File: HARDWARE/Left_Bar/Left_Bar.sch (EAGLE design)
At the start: 13 parts, among them J1 TRRS

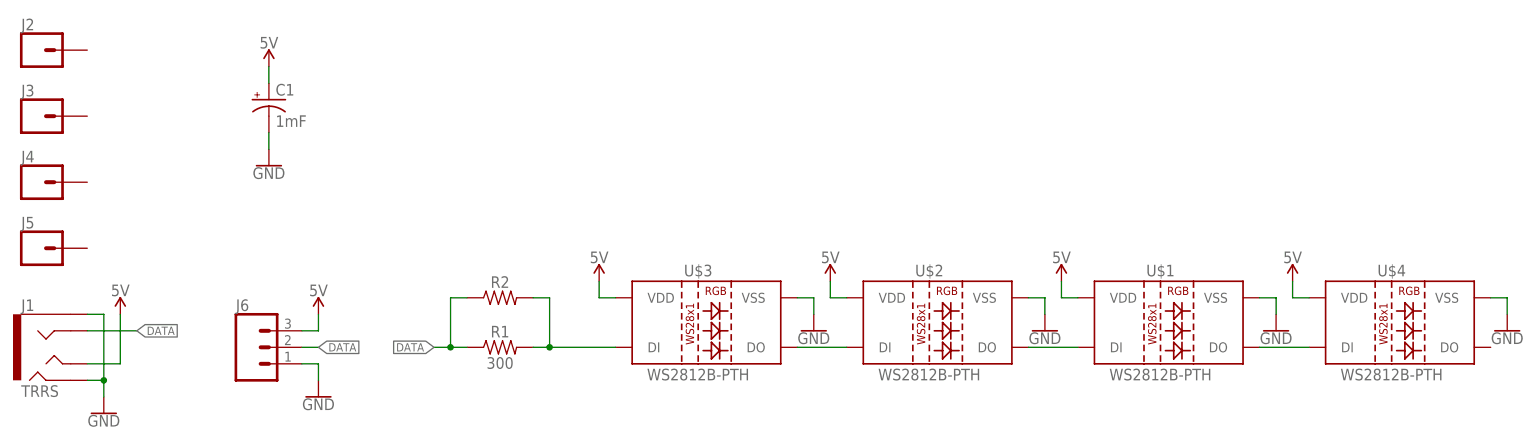
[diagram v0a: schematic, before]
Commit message: renames right and left, finished left
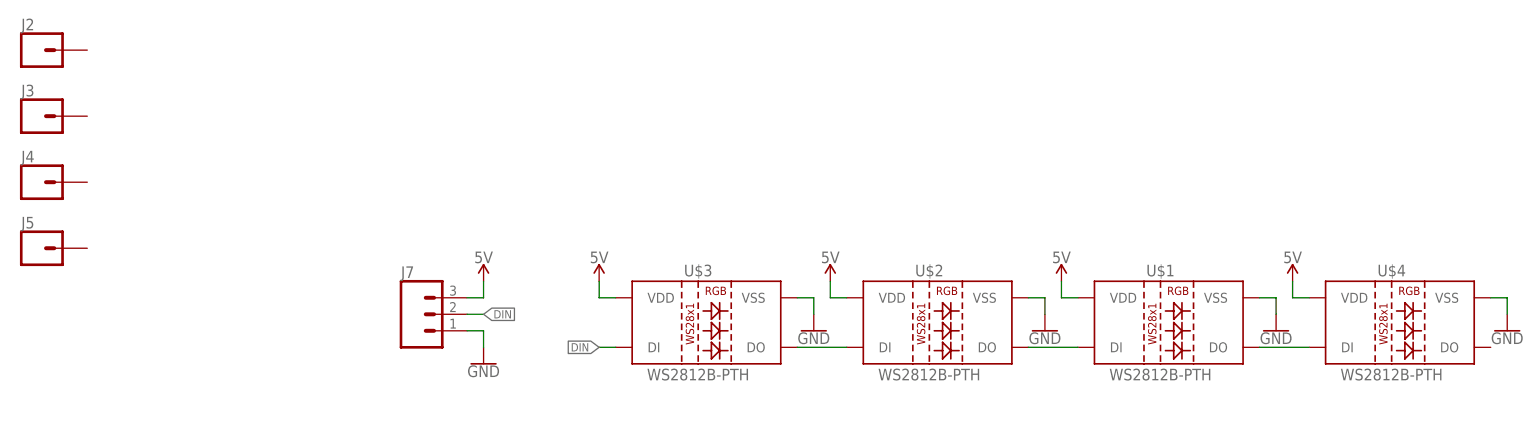
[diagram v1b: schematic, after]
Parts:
- removed C1: 1mF, SparkFun-Capacitors:1000UF-RADIAL-5MM-25V-20%
- removed J1: TRRS, SparkFun-Connectors:AUDIO_JACK_TRRSSMD_RA
- removed J6: (no value), SparkFun-Connectors:CONN_03
- removed R1: 300, SparkFun-Resistors:300OHM-0603-1/10W-1%
- removed R2: (no value), SparkFun-Resistors:RESISTORAXIAL-0.3
- added J7: (no value), SparkFun-Connectors:CONN_03
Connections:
- removed net DATA: J1.RING1, J6.2, R1.1, R2.1
- removed net N$2: R1.2, R2.2, U$3.DI
- new net DIN: J7.2, U$3.DI
- net 5V: now also J7.3; no longer C1.+, J1.TIP, J6.3
- net GND: now also J7.1; no longer C1.-, J1.EARTH, J1.RING2, J6.1
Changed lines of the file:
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@@
 </classes>
 <parts>
-<part name="J1" library="SparkFun-Connectors" deviceset="AUDIO_JACK_TRRS" device="SMD_RA" value="TRRS"/>
 <part name="U$1" library="SparkFun-LED" deviceset="WS2812B-PTH" device=""/>
 <part name="U$2" library="SparkFun-LED" deviceset="WS2812B-PTH" device=""/>
@@
 <part name="J4" library="SparkFun-Connectors" deviceset="CONN_01" device="OFFSET"/>
 <part name="J5" library="SparkFun-Connectors" deviceset="CONN_01" device="OFFSET"/>
-<part name="J6" library="SparkFun-Connectors" deviceset="CONN_03" device=""/>
 <part name="SUPPLY1" library="SparkFun-PowerSymbols" deviceset="5V" device=""/>
 <part name="SUPPLY2" library="SparkFun-PowerSymbols" deviceset="5V" device=""/>
 <part name="SUPPLY3" library="SparkFun-PowerSymbols" deviceset="5V" device=""/>
-<part name="SUPPLY4" library="SparkFun-PowerSymbols" deviceset="5V" device=""/>
-<part name="GND1" library="SparkFun-PowerSymbols" deviceset="GND" device=""/>
 <part name="GND2" library="SparkFun-PowerSymbols" deviceset="GND" device=""/>
 <part name="GND3" library="SparkFun-PowerSymbols" deviceset="GND" device=""/>
 <part name="GND4" library="SparkFun-PowerSymbols" deviceset="GND" device=""/>
-<part name="GND5" library="SparkFun-PowerSymbols" deviceset="GND" device=""/>
-<part name="SUPPLY5" library="SparkFun-PowerSymbols" deviceset="5V" device=""/>
 <part name="U$4" library="SparkFun-LED" deviceset="WS2812B-PTH" device=""/>
 <part name="SUPPLY6" library="SparkFun-PowerSymbols" deviceset="5V" device=""/>
 <part name="GND6" library="SparkFun-PowerSymbols" deviceset="GND" device=""/>
-<part name="R1" library="SparkFun-Resistors" deviceset="300OHM" device="-0603-1/10W-1%" value="300"/>
-<part name="R2" library="SparkFun-Resistors" deviceset="RESISTOR" device="AXIAL-0.3" value=" "/>
-<part name="C1" library="SparkFun-Capacitors" deviceset="1000UF" device="-RADIAL-5MM-25V-20%" value="1mF"/>
-<part name="GND7" library="SparkFun-PowerSymbols" deviceset="GND" device=""/>
-<part name="SUPPLY7" library="SparkFun-PowerSymbols" deviceset="5V" device=""/>
+<part name="J7" library="SparkFun-Connectors" deviceset="CONN_03" device=""/>
+<part name="GND8" library="SparkFun-PowerSymbols" deviceset="GND" device=""/>
+<part name="SUPPLY8" library="SparkFun-PowerSymbols" deviceset="5V" device=""/>
 </parts>
 <sheets>
@@
 </plain>
 <instances>
-<instance part="J1" gate="G$1" x="40.64" y="55.88"/>
 <instance part="U$1" gate="G$1" x="213.36" y="58.42"/>
 <instance part="U$2" gate="G$1" x="177.8" y="58.42"/>
@@
 <instance part="J4" gate="G$1" x="38.1" y="81.28"/>
 <instance part="J5" gate="G$1" x="38.1" y="71.12"/>
-<instance part="J6" gate="J$1" x="71.12" y="55.88"/>
 <instance part="SUPPLY1" gate="G$1" x="124.46" y="66.04"/>
 <instance part="SUPPLY2" gate="G$1" x="160.02" y="66.04"/>
 <instance part="SUPPLY3" gate="G$1" x="195.58" y="66.04"/>
-<instance part="SUPPLY4" gate="G$1" x="50.8" y="60.96"/>
-<instance part="GND1" gate="1" x="48.26" y="45.72"/>
 <instance part="GND2" gate="1" x="157.48" y="58.42"/>
 <instance part="GND3" gate="1" x="193.04" y="58.42"/>
 <instance part="GND4" gate="1" x="228.6" y="58.42"/>
-<instance part="GND5" gate="1" x="81.28" y="48.26"/>
-<instance part="SUPPLY5" gate="G$1" x="81.28" y="60.96"/>
 <instance part="U$4" gate="G$1" x="248.92" y="58.42"/>
 <instance part="SUPPLY6" gate="G$1" x="231.14" y="66.04"/>
 <instance part="GND6" gate="1" x="264.16" y="58.42"/>
-<instance part="R1" gate="G$1" x="109.22" y="55.88"/>
-<instance part="R2" gate="G$1" x="109.22" y="63.5"/>
-<instance part="C1" gate="G$1" x="73.66" y="93.98"/>
-<instance part="GND7" gate="1" x="73.66" y="83.82"/>
-<instance part="SUPPLY7" gate="G$1" x="73.66" y="99.06"/>
+<instance part="J7" gate="J$1" x="96.52" y="60.96"/>
+<instance part="GND8" gate="1" x="106.68" y="53.34"/>
+<instance part="SUPPLY8" gate="G$1" x="106.68" y="66.04"/>
 </instances>
 <busses>
@@
 </segment>
 <segment>
-<pinref part="SUPPLY4" gate="G$1" pin="5V"/>
-<wire x1="50.8" y1="58.42" x2="50.8" y2="60.96" width="0.1524" layer="91"/>
-<wire x1="50.8" y1="58.42" x2="50.8" y2="53.34" width="0.1524" layer="91"/>
-<pinref part="J1" gate="G$1" pin="TIP"/>
-<wire x1="50.8" y1="53.34" x2="45.72" y2="53.34" width="0.1524" layer="91"/>
-</segment>
-<segment>
-<pinref part="J6" gate="J$1" pin="3"/>
-<wire x1="78.74" y1="58.42" x2="81.28" y2="58.42" width="0.1524" layer="91"/>
-<pinref part="SUPPLY5" gate="G$1" pin="5V"/>
-<wire x1="81.28" y1="58.42" x2="81.28" y2="60.96" width="0.1524" layer="91"/>
-</segment>
-<segment>
 <pinref part="U$4" gate="G$1" pin="VDD"/>
 <wire x1="233.68" y1="63.5" x2="231.14" y2="63.5" width="0.1524" layer="91"/>
@@
 </segment>
 <segment>
-<pinref part="SUPPLY7" gate="G$1" pin="5V"/>
-<wire x1="73.66" y1="96.52" x2="73.66" y2="99.06" width="0.1524" layer="91"/>
-<pinref part="C1" gate="G$1" pin="+"/>
+<pinref part="J7" gate="J$1" pin="3"/>
+<wire x1="104.14" y1="63.5" x2="106.68" y2="63.5" width="0.1524" layer="91"/>
+<pinref part="SUPPLY8" gate="G$1" pin="5V"/>
+<wire x1="106.68" y1="63.5" x2="106.68" y2="66.04" width="0.1524" layer="91"/>
 </segment>
 </net>
@@
 </segment>
 <segment>
-<pinref part="J1" gate="G$1" pin="EARTH"/>
-<wire x1="45.72" y1="60.96" x2="48.26" y2="60.96" width="0.1524" layer="91"/>
-<wire x1="48.26" y1="60.96" x2="48.26" y2="50.8" width="0.1524" layer="91"/>
-<pinref part="J1" gate="G$1" pin="RING2"/>
-<wire x1="48.26" y1="50.8" x2="48.26" y2="48.26" width="0.1524" layer="91"/>
-<wire x1="45.72" y1="50.8" x2="48.26" y2="50.8" width="0.1524" layer="91"/>
-<junction x="48.26" y="50.8"/>
-<pinref part="GND1" gate="1" pin="GND"/>
-</segment>
-<segment>
-<pinref part="J6" gate="J$1" pin="1"/>
-<wire x1="78.74" y1="53.34" x2="81.28" y2="53.34" width="0.1524" layer="91"/>
-<pinref part="GND5" gate="1" pin="GND"/>
-<wire x1="81.28" y1="53.34" x2="81.28" y2="50.8" width="0.1524" layer="91"/>
-</segment>
-<segment>
 <pinref part="U$4" gate="G$1" pin="VSS"/>
 <wire x1="261.62" y1="63.5" x2="264.16" y2="63.5" width="0.1524" layer="91"/>
@@
 </segment>
 <segment>
-<pinref part="C1" gate="G$1" pin="-"/>
-<pinref part="GND7" gate="1" pin="GND"/>
-<wire x1="73.66" y1="86.36" x2="73.66" y2="88.9" width="0.1524" layer="91"/>
-</segment>
-</net>
-<net name="DATA" class="0">
-<segment>
-<pinref part="J6" gate="J$1" pin="2"/>
-<wire x1="78.74" y1="55.88" x2="81.28" y2="55.88" width="0.1524" layer="91"/>
-<label x="81.28" y="55.88" size="1.27" layer="95" xref="yes"/>
-</segment>
-<segment>
-<pinref part="J1" gate="G$1" pin="RING1"/>
-<wire x1="45.72" y1="58.42" x2="53.34" y2="58.42" width="0.1524" layer="91"/>
-<label x="53.34" y="58.42" size="1.27" layer="95" xref="yes"/>
-</segment>
-<segment>
-<wire x1="104.14" y1="55.88" x2="101.6" y2="55.88" width="0.1524" layer="91"/>
-<label x="99.06" y="55.88" size="1.27" layer="95" rot="R180" xref="yes"/>
-<pinref part="R1" gate="G$1" pin="1"/>
-<pinref part="R2" gate="G$1" pin="1"/>
-<wire x1="101.6" y1="55.88" x2="99.06" y2="55.88" width="0.1524" layer="91"/>
-<wire x1="104.14" y1="63.5" x2="101.6" y2="63.5" width="0.1524" layer="91"/>
-<wire x1="101.6" y1="63.5" x2="101.6" y2="55.88" width="0.1524" layer="91"/>
-<junction x="101.6" y="55.88"/>
+<pinref part="J7" gate="J$1" pin="1"/>
+<wire x1="104.14" y1="58.42" x2="106.68" y2="58.42" width="0.1524" layer="91"/>
+<pinref part="GND8" gate="1" pin="GND"/>
+<wire x1="106.68" y1="58.42" x2="106.68" y2="55.88" width="0.1524" layer="91"/>
 </segment>
 </net>
@@
 </segment>
 </net>
-<net name="N$2" class="0">
+<net name="DIN" class="0">
+<segment>
+<pinref part="J7" gate="J$1" pin="2"/>
+<wire x1="104.14" y1="60.96" x2="106.68" y2="60.96" width="0.1524" layer="91"/>
+<label x="106.68" y="60.96" size="1.27" layer="95" rot="MR180" xref="yes"/>
+</segment>
 <segment>
 <pinref part="U$3" gate="G$1" pin="DI"/>
-<pinref part="R1" gate="G$1" pin="2"/>
-<wire x1="127" y1="55.88" x2="116.84" y2="55.88" width="0.1524" layer="91"/>
-<wire x1="116.84" y1="55.88" x2="114.3" y2="55.88" width="0.1524" layer="91"/>
-<wire x1="116.84" y1="55.88" x2="116.84" y2="63.5" width="0.1524" layer="91"/>
-<junction x="116.84" y="55.88"/>
-<pinref part="R2" gate="G$1" pin="2"/>
-<wire x1="116.84" y1="63.5" x2="114.3" y2="63.5" width="0.1524" layer="91"/>
+<wire x1="127" y1="55.88" x2="124.46" y2="55.88" width="0.1524" layer="91"/>
+<label x="124.46" y="55.88" size="1.27" layer="95" rot="R180" xref="yes"/>
 </segment>
 </net>
